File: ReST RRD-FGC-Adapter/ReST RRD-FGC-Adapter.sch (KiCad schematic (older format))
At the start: 18 parts, among them P1 CONN_02X05, P2 CONN_02X05, P3 CONN_02X05, P4 CONN_02X05, Q1 BSS138, Q2 BSS138, Q3 BSS138, Q4 BSS138, U1 MIC5205

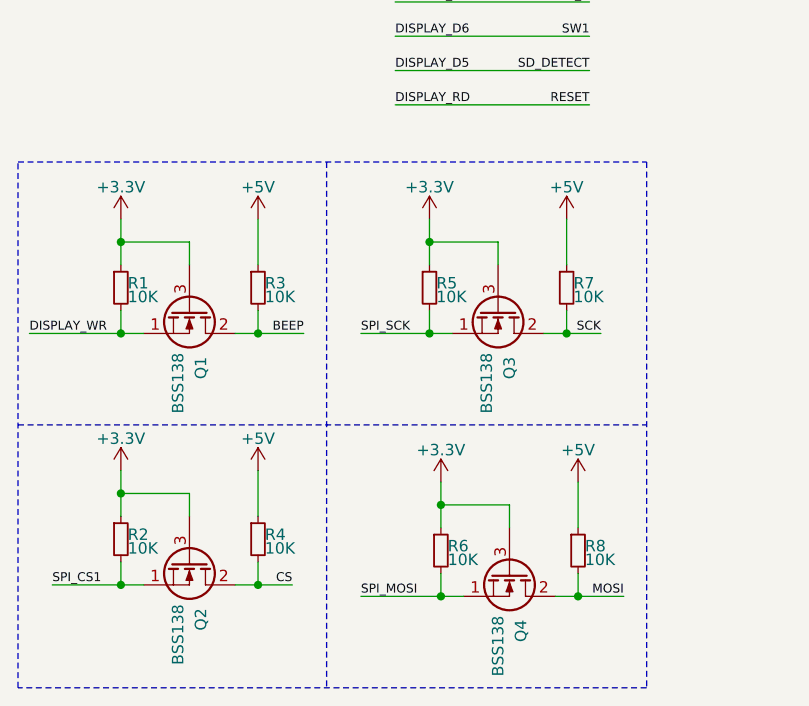
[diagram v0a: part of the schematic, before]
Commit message: now using a 74ahc125 instead of transistor logic for level conversion
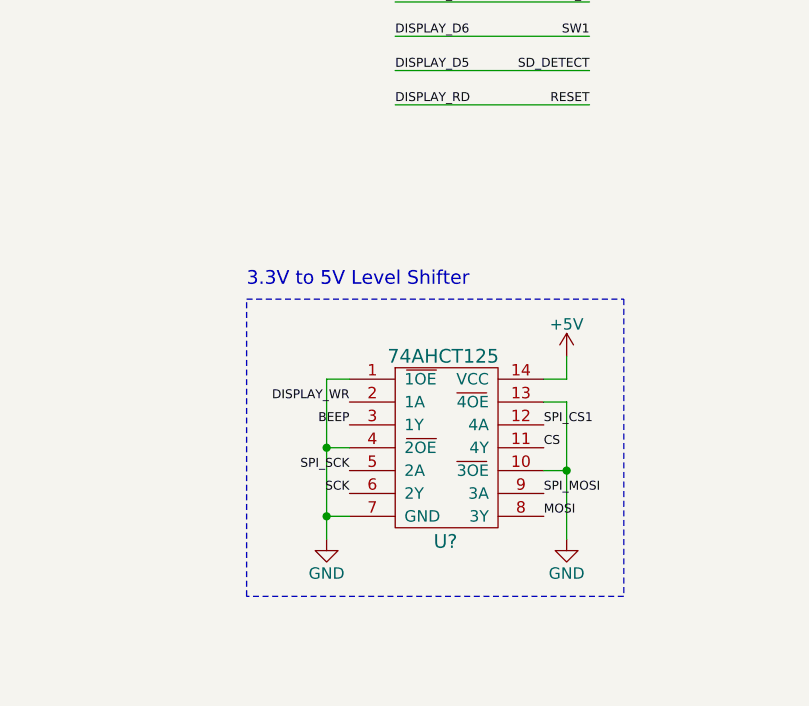
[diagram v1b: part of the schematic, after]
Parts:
- removed Q1, Q2, Q3, Q4: BSS138, TO_SOT_Packages_SMD:SOT-23_Handsoldering, symbol Q_NMOS_SDG
- removed R1, R2, R3, R4, R5, R6, R7, R8: 10K, Resistors_SMD:R_0805_HandSoldering, symbol R_Small
- added U?: 74AHCT125, Housings_SSOP:TSSOP-14_4.4x5mm_Pitch0.65mm, symbol 74AHCT125
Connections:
- net +5V: now also U?.14 (VCC)
- net BEEP: now also U?.3 (1Y)
- net CS: now also U?.11 (4Y)
- net DISPLAY_WR: now also U?.2 (1A)
- net GND: now also U?.1 (1OE), U?.10 (3OE), U?.13 (4OE), U?.4 (2OE), U?.7 (GND)
- net MOSI: now also U?.8 (3Y)
- net SCK: now also U?.6 (2Y)
- net SPI_CS1: now also U?.12 (4A)
- net SPI_MOSI: now also U?.9 (3A)
- net SPI_SCK: now also U?.5 (2A)
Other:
- note added: "3.3V to 5V Level Shifter"
